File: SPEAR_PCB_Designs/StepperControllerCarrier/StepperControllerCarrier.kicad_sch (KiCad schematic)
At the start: 17 parts, among them J1 Conn_01x02_Pin, J2 Conn_01x02_Pin, J3 Conn_01x02_Pin, J4 Conn_01x04_Pin, U1 AP63203WU

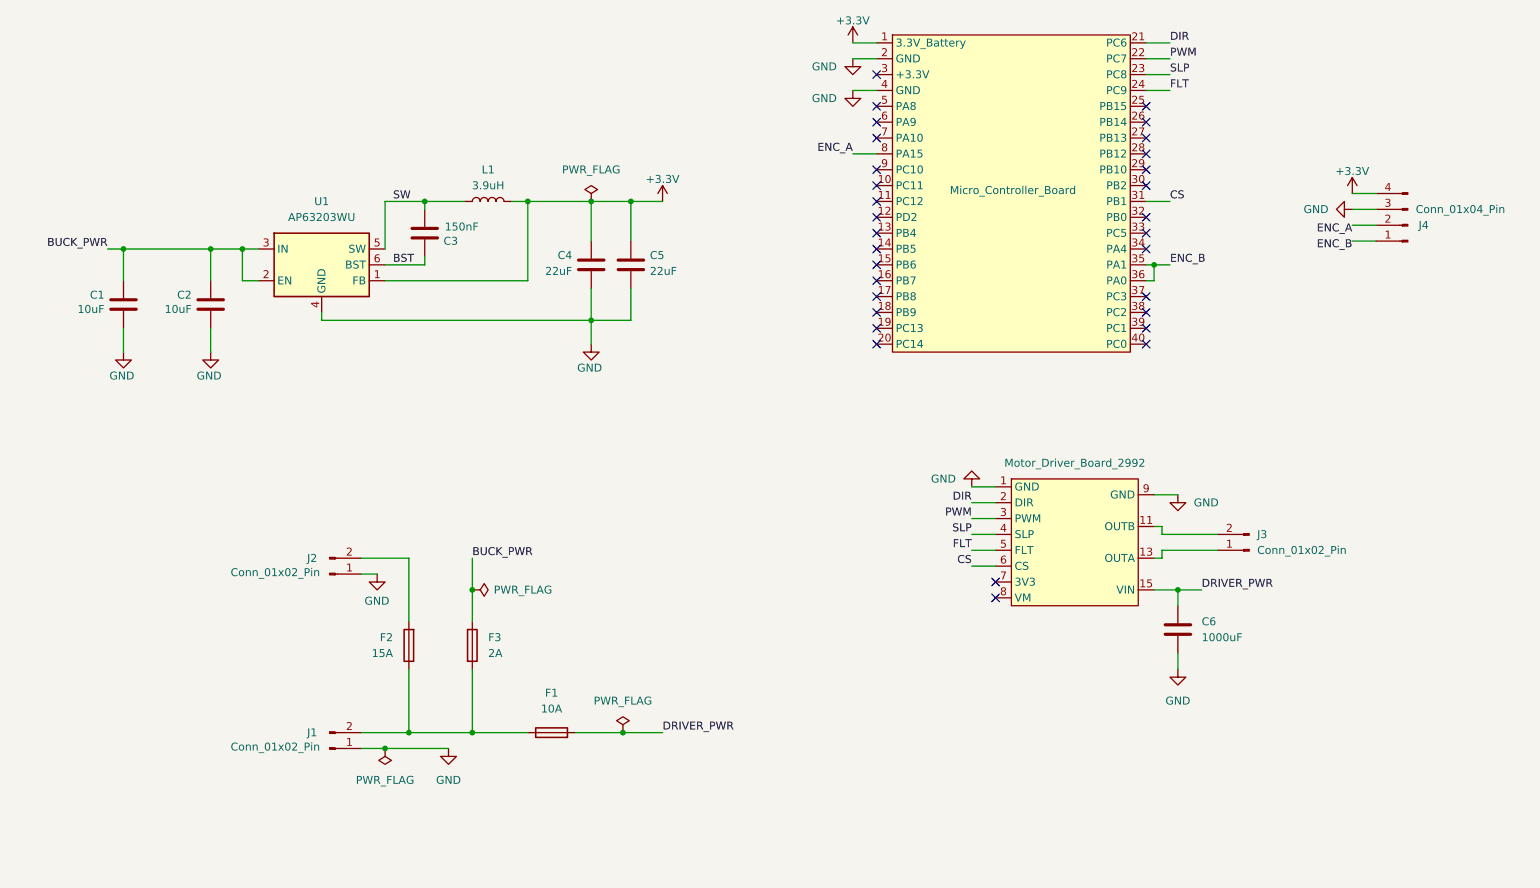
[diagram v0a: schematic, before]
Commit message: Routed traces for unconnected pins on stepper motor driver and did some organizing
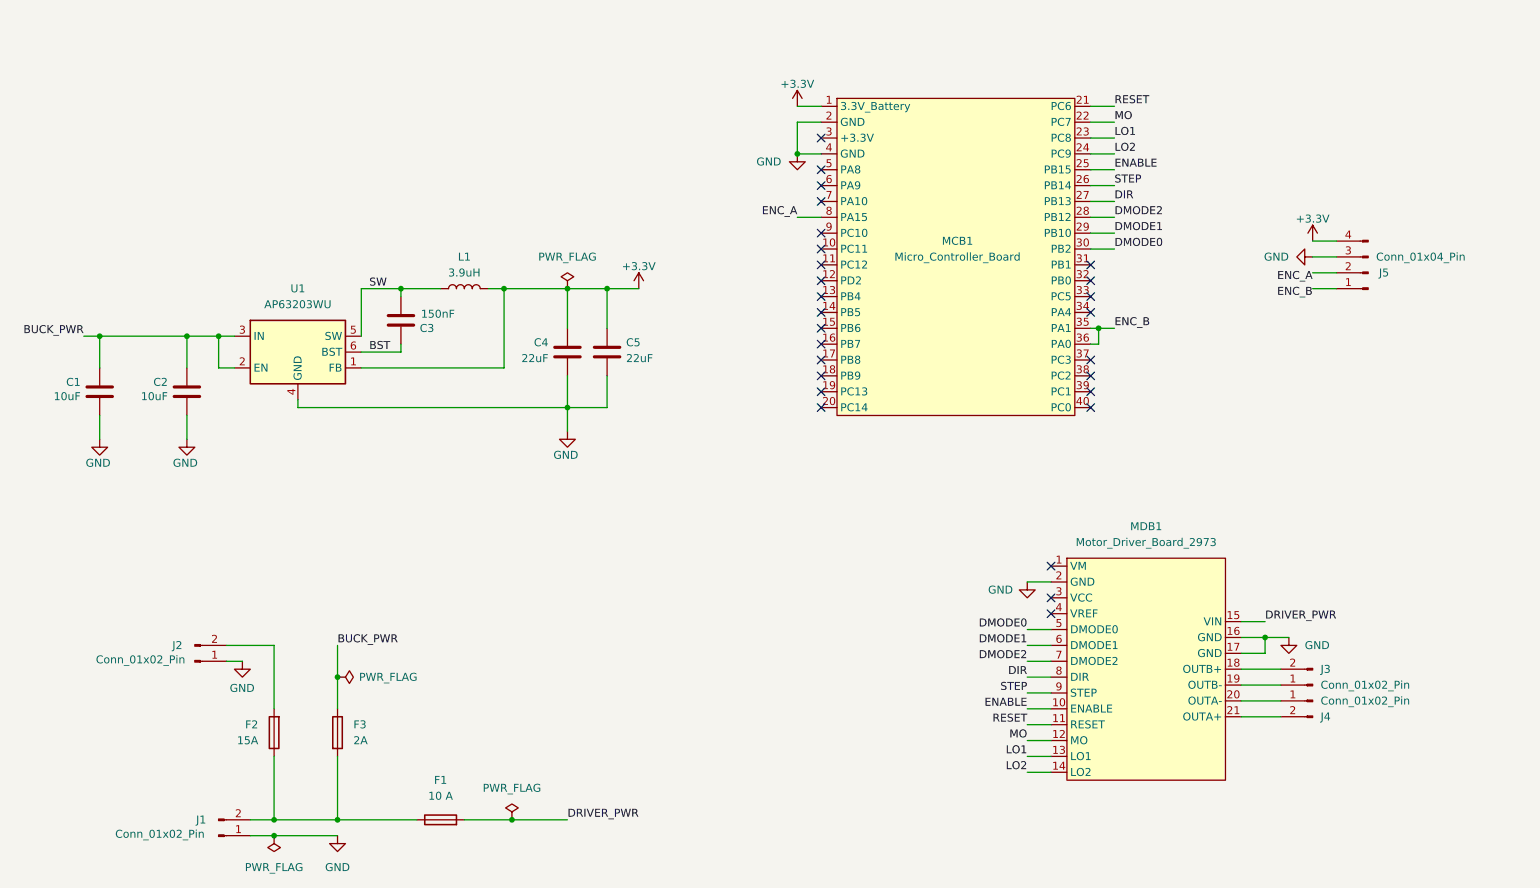
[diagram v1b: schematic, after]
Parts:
- removed C6: 1000uF, Motor_Controller_Carrier_Board:CAP_UBY_18X20_NCH, symbol Device:C
- removed F2: 15A, Motor_Controller_Carrier_Board:FUSE_3557-15, symbol Motor_Controller_Carrier_Board:Fuse_2Pin
- removed J4: Conn_01x04_Pin, SPEAR_Connectors:JST_XH_S4B-XH-A-1_1x04_P2.50mm_Horizontal, symbol Connector:Conn_01x04_Pin
- removed MDB1: Motor_Driver_Board_2992, SPEAR_Boards:Motor_Driver_Board_2992, symbol SPEAR_Boards:Motor_Driver_Board_2992
- added F2: 15A, SPEAR_MotorControllerCarrier:FUSE_3557-15, symbol SPEAR_MotorControllerCarrier:Fuse_2Pin
- added J4: Conn_01x02_Pin, Connector_AMASS:AMASS_XT30PW-M_1x02_P2.50mm_Horizontal, symbol Connector:Conn_01x02_Pin
- added J5: Conn_01x04_Pin, SPEAR_Connectors:JST_XH_S4B-XH-A-1_1x04_P2.50mm_Horizontal, symbol Connector:Conn_01x04_Pin
- added MDB1: Motor_Driver_Board_2973, SPEAR_Boards:Motor_Driver_Board_2973, symbol SPEAR_Boards:Motor_Driver_Board_2973
- C1, C2: footprint Motor_Controller_Carrier_Board:CAPC3225X270N -> SPEAR_MotorControllerCarrier:CAPC3225X270N
- C3: footprint Motor_Controller_Carrier_Board:CAP_CC1206_YAG -> SPEAR_MotorControllerCarrier:CAP_CC1206_YAG
- C4, C5: footprint Motor_Controller_Carrier_Board:CAP_C3225X7R1C226M250AC -> SPEAR_MotorControllerCarrier:CAP_C3225X7R1C226M250AC
- F1: value 10A -> 10 A; footprint Motor_Controller_Carrier_Board:FUSE_3557-10 -> SPEAR_MotorControllerCarrier:FUSE_3557-10; symbol Motor_Controller_Carrier_Board:Fuse_2Pin -> SPEAR_MotorControllerCarrier:Fuse_2Pin
- F3: footprint Motor_Controller_Carrier_Board:FUS_LITTELFUSE_392_LTF -> SPEAR_MotorControllerCarrier:FUS_LITTELFUSE_392_LTF
- J1, J3: footprint SPEAR_Connectors:AMASS_XT30PW-M_1x02_P2.50mm_Horizontal_1 -> Connector_AMASS:AMASS_XT30PW-M_1x02_P2.50mm_Horizontal; now in the parts list
- U1: footprint Motor_Controller_Carrier_Board:TSOT-23-6 -> SPEAR_MotorControllerCarrier:TSOT-23-6
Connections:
- net +3.3V: now also J5.4 (Pin_4)
- net DIR: now also MCB1.27 (PB13), MDB1.8 (DIR); no longer MCB1.21 (PC6)
- net DRIVER_PWR: now also MDB1.15 (VIN)
- net ENC_A: now also J5.2 (Pin_2)
- net ENC_B: now also J5.1 (Pin_1)
- net GND: now also J5.3 (Pin_3), MDB1.16 (GND), MDB1.17 (GND), MDB1.2 (GND)
- net at J3.1 (Pin_1): now also MDB1.19 (OUTB-)
- net at J3.2 (Pin_2): now also MDB1.18 (OUTB+)
- net ENABLE: now reaches MCB1.25 (PB15)
- net ENABLE: now also MDB1.10 (ENABLE)
- net STEP: now reaches MCB1.26 (PB14)
- net STEP: now also MDB1.9 (STEP)
- net DMODE2: now reaches MCB1.28 (PB12)
- net DMODE2: now also MDB1.7 (DMODE2)
- net DMODE1: now reaches MCB1.29 (PB10)
- net DMODE1: now also MDB1.6 (DMODE1)
- net DMODE0: now reaches MCB1.30 (PB2)
- net DMODE0: now also MDB1.5 (DMODE0)
- net at F1.1_1, F1.1_2, F3.2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: now also F2.1_1, F2.1_2
- net at J2.2 (Pin_2): now also F2.2_1, F2.2_2
- net CS: no longer names the net of MCB1.31 (PB1)
- net FLT renamed LO2
- net LO2: now also MDB1.14 (LO2)
- net PWM renamed MO
- net MO: now also MDB1.12 (MO)
- net SLP renamed LO1
- net LO1: now also MDB1.13 (LO1)
- new net: J4.1 (Pin_1), MDB1.20 (OUTA-)
- new net: J4.2 (Pin_2), MDB1.21 (OUTA+)
- new net RESET: MCB1.21 (PC6), MDB1.11 (RESET)
- no-connect marks 31 -> 27
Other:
- company: (none) -> SPEAR
- title: (none) -> Motor Controller Carrier Board
- moved on the sheet: F1, J1

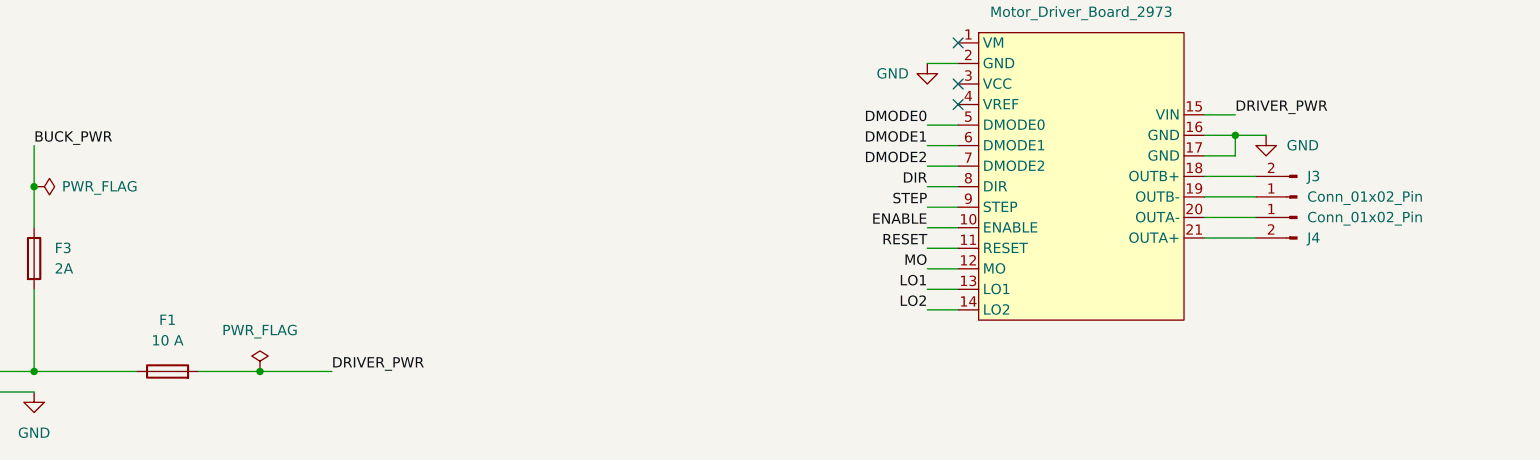
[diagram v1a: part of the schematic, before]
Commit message: Moved mounting hole on stepper controller carrier
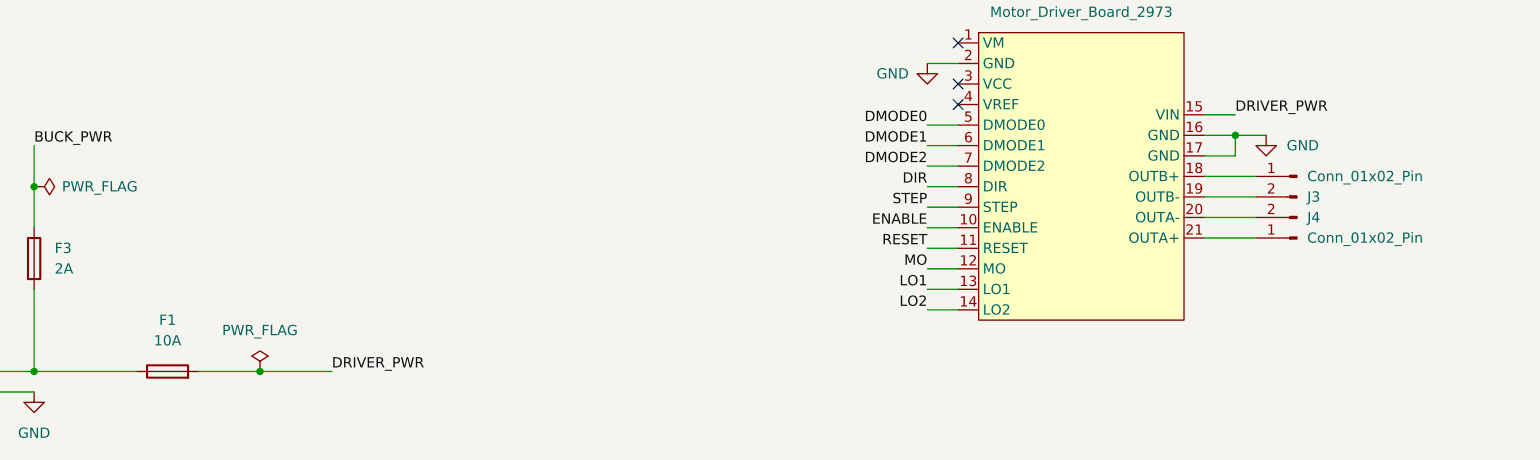
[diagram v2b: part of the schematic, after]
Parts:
- F1: value 10 A -> 10A
- J1, J3, J4: footprint Connector_AMASS:AMASS_XT30PW-M_1x02_P2.50mm_Horizontal -> SPEAR_Connectors:AMASS_XT30PW-M_1x02_P2.50mm_Horizontal_1
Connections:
- net at J3.1 (Pin_1): now also MDB1.18 (OUTB+); no longer MDB1.19 (OUTB-)
- net at J3.2 (Pin_2): now also MDB1.19 (OUTB-); no longer MDB1.18 (OUTB+)
- net at MDB1.20 (OUTA-): now also J4.2 (Pin_2); no longer J4.1 (Pin_1)
- net at MDB1.21 (OUTA+): now also J4.1 (Pin_1); no longer J4.2 (Pin_2)
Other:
- moved on the sheet: J3, J4
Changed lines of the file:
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@@
 	(symbol
 		(lib_id "Connector:Conn_01x02_Pin")
-		(at 232.41 140.97 180)
+		(at 232.41 138.43 0)
+		(mirror y)
 		(unit 1)
 		(exclude_from_sim no)
@@
 		(dnp no)
 		(property "Reference" "J3"
-			(at 233.68 138.4299 0)
+			(at 233.68 140.9701 0)
 			(effects
 				(font
@@
 		)
 		(property "Value" "Conn_01x02_Pin"
-			(at 233.68 140.9699 0)
+			(at 233.68 138.4301 0)
 			(effects
 				(font
@@
 			)
 		)
-		(property "Footprint" "Connector_AMASS:AMASS_XT30PW-M_1x02_P2.50mm_Horizontal"
-			(at 232.41 140.97 0)
+		(property "Footprint" "SPEAR_Connectors:AMASS_XT30PW-M_1x02_P2.50mm_Horizontal_1"
+			(at 232.41 138.43 0)
 			(effects
 				(font
@@
 		)
 		(property "Datasheet" "~"
-			(at 232.41 140.97 0)
+			(at 232.41 138.43 0)
 			(effects
 				(font
@@
 		)
 		(property "Description" "Generic connector, single row, 01x02, script generated"
-			(at 232.41 140.97 0)
+			(at 232.41 138.43 0)
 			(effects
 				(font
@@
 		)
 		(property "DigiKey_Part_Number" ""
-			(at 232.41 140.97 0)
+			(at 232.41 138.43 0)
 			(effects
 				(font
@@
 		)
 		(instances
-			(project "Stepper_Motor_Controller_Carrier_Board"
+			(project "StepperControllerCarrier"
 				(path "/f3c97344-c35a-4a43-a333-44ea37de3455"
 					(reference "J3")
@@
 			)
 		)
-		(property "Footprint" "Connector_AMASS:AMASS_XT30PW-M_1x02_P2.50mm_Horizontal"
+		(property "Footprint" "SPEAR_Connectors:AMASS_XT30PW-M_1x02_P2.50mm_Horizontal_1"
 			(at 57.15 165.1 0)
 			(effects
@@
 	(symbol
 		(lib_id "Connector:Conn_01x02_Pin")
-		(at 232.41 143.51 0)
-		(mirror y)
+		(at 232.41 146.05 180)
 		(unit 1)
 		(exclude_from_sim no)
@@
 		(dnp no)
 		(property "Reference" "J4"
-			(at 233.68 146.0501 0)
+			(at 233.68 143.5099 0)
 			(effects
 				(font
@@
 		)
 		(property "Value" "Conn_01x02_Pin"
-			(at 233.68 143.5101 0)
+			(at 233.68 146.0499 0)
 			(effects
 				(font
@@
 			)
 		)
-		(property "Footprint" "Connector_AMASS:AMASS_XT30PW-M_1x02_P2.50mm_Horizontal"
-			(at 232.41 143.51 0)
+		(property "Footprint" "SPEAR_Connectors:AMASS_XT30PW-M_1x02_P2.50mm_Horizontal_1"
+			(at 232.41 146.05 0)
 			(effects
 				(font
@@
 		)
 		(property "Datasheet" "~"
-			(at 232.41 143.51 0)
+			(at 232.41 146.05 0)
 			(effects
 				(font
@@
 		)
 		(property "Description" "Generic connector, single row, 01x02, script generated"
-			(at 232.41 143.51 0)
+			(at 232.41 146.05 0)
 			(effects
 				(font
@@
 		)
 		(property "DigiKey_Part_Number" ""
-			(at 232.41 143.51 0)
+			(at 232.41 146.05 0)
 			(effects
 				(font
@@
 		)
 		(instances
-			(project "Stepper_Motor_Controller_Carrier_Board"
+			(project "StepperControllerCarrier"
 				(path "/f3c97344-c35a-4a43-a333-44ea37de3455"
 					(reference "J4")
@@
 			)
 		)
-		(property "Value" "10 A"
+		(property "Value" "10A"
 			(at 92.71 158.75 0)
 			(effects
